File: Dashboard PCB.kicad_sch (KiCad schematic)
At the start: 32 parts, among them J1 Controls_Leader_Export_02x06, J2 Conn_01x02, J3 Conn_01x02, J4 FAN_CTRL_01x02

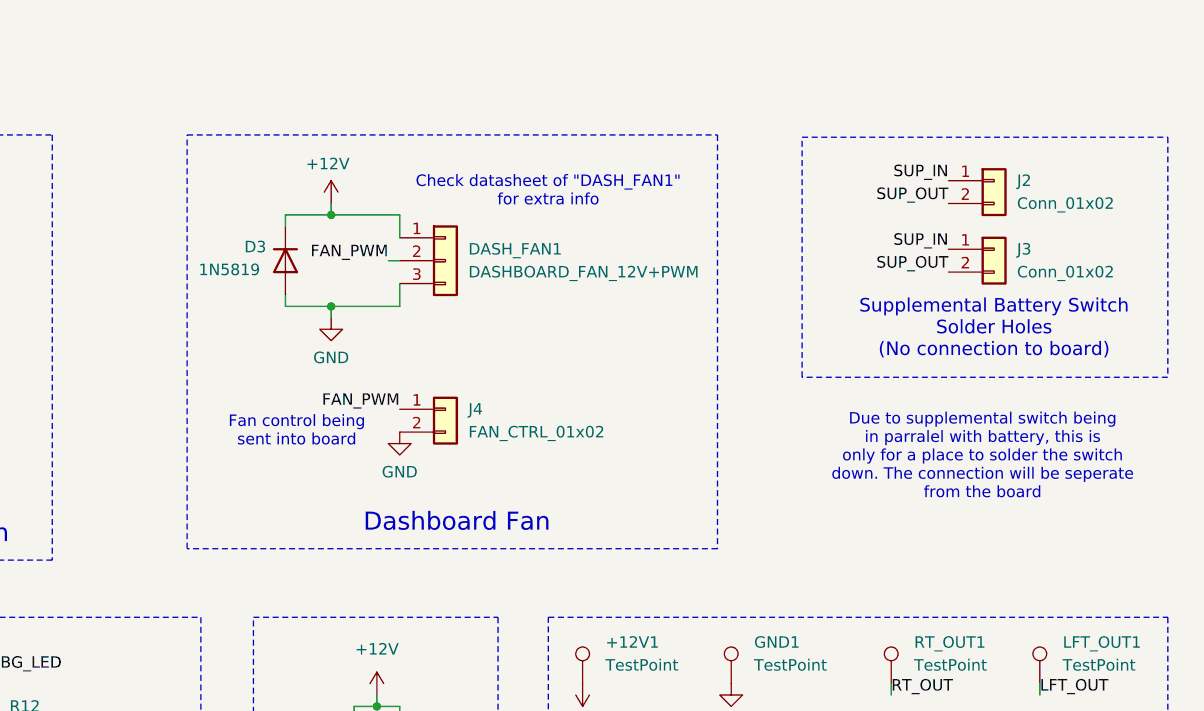
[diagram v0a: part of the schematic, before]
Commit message: Started assigning footprints
Still have a few missing, and not sure if im doing it all right
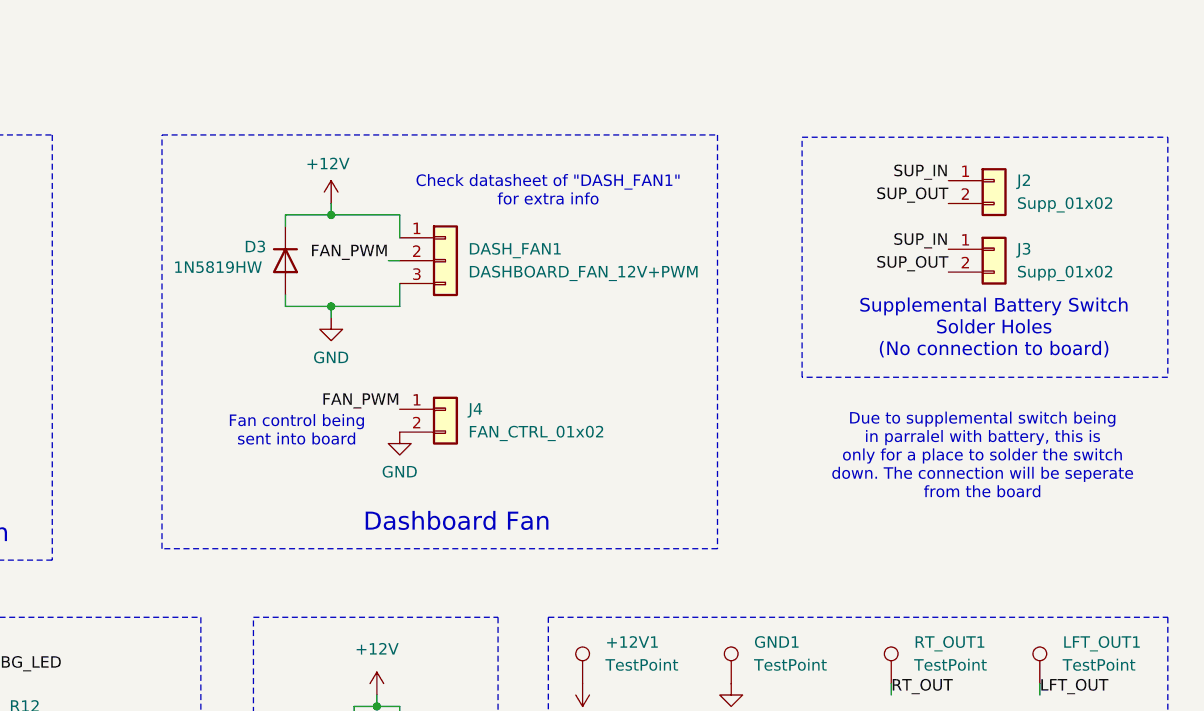
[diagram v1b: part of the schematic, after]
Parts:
- +12V1, CRUZ_EN1, CRUZ_SET1, DBG_LED1, FAN_PWM1, FWD_SW1, GND1, IGN_ARR1, IGN_PWR1, LFT_OUT1, REV_SW1, RT_OUT1: footprint (none) -> TestPoint:TestPoint_Plated_Hole_D3.0mm
- D3: value 1N5819 -> 1N5819HW; footprint (none) -> Diode_SMD:D_SOD-123
- DASH_FAN1: footprint (none) -> Connector_Molex:Molex_Micro-Fit_3.0_43650-0300_1x03_P3.00mm_Horizontal
- Heartbeat_LED1, LFT_LED1, RT_LED1: footprint (none) -> LED_SMD:LED_0805_2012Metric
- J1: footprint (none) -> Connector_Molex:Molex_Micro-Fit_3.0_43045-1200_2x06_P3.00mm_Horizontal
- J2, J3: value Conn_01x02 -> Supp_01x02
- J4: footprint (none) -> Connector_Molex:Molex_Micro-Fit_3.0_43650-0200_1x02_P3.00mm_Horizontal
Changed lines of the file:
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@@
 	)
 	(rectangle
-		(start 147.828 60.96)
+		(start 145.034 60.96)
 		(end 206.756 106.934)
 		(stroke
@@
 			)
 		)
-		(property "Footprint" ""
+		(property "Footprint" "TestPoint:TestPoint_Plated_Hole_D3.0mm"
 			(at 213.36 121.92 0)
 			(effects
@@
 			)
 		)
-		(property "Footprint" ""
+		(property "Footprint" "LED_SMD:LED_0805_2012Metric"
 			(at 97.79 133.35 0)
 			(effects
@@
 			)
 		)
-		(property "Footprint" ""
+		(property "Footprint" "TestPoint:TestPoint_Plated_Hole_D3.0mm"
 			(at 247.65 134.62 0)
 			(effects
@@
 			)
 		)
-		(property "Footprint" ""
+		(property "Footprint" "Connector_Molex:Molex_Micro-Fit_3.0_43650-0200_1x02_P3.00mm_Horizontal"
 			(at 176.53 91.44 0)
 			(effects
@@
 			)
 		)
-		(property "Value" "Conn_01x02"
+		(property "Value" "Supp_01x02"
 			(at 240.03 68.5799 0)
 			(effects
@@
 			)
 		)
-		(property "Footprint" ""
+		(property "Footprint" "TestPoint:TestPoint_Plated_Hole_D3.0mm"
 			(at 196.85 147.32 0)
 			(effects
@@
 			)
 		)
-		(property "Value" "Conn_01x02"
+		(property "Value" "Supp_01x02"
 			(at 240.03 76.1999 0)
 			(effects
@@
 			)
 		)
-		(property "Footprint" ""
+		(property "Footprint" "LED_SMD:LED_0805_2012Metric"
 			(at 71.12 133.35 0)
 			(effects
@@
 			)
 		)
-		(property "Footprint" ""
+		(property "Footprint" "TestPoint:TestPoint_Plated_Hole_D3.0mm"
 			(at 231.14 147.32 0)
 			(effects
@@
 			)
 		)
-		(property "Footprint" ""
+		(property "Footprint" "TestPoint:TestPoint_Plated_Hole_D3.0mm"
 			(at 213.36 147.32 0)
 			(effects
@@
 			)
 		)
-		(property "Value" "1N5819"
-			(at 149.098 75.946 90)
+		(property "Value" "1N5819HW"
+			(at 146.304 75.692 90)
 			(effects
 				(font
@@
 			)
 		)
-		(property "Footprint" ""
+		(property "Footprint" "Diode_SMD:D_SOD-123"
 			(at 158.75 74.93 0)
 			(effects
@@
 			)
 		)
-		(property "Datasheet" "~"
+		(property "Datasheet" "https://www.digikey.com/en/products/detail/diodes-incorporated/1N5819HW-7-F/814970"
 			(at 158.75 74.93 0)
 			(effects
@@
 			)
 		)
-		(property "Footprint" ""
+		(property "Footprint" "TestPoint:TestPoint_Plated_Hole_D3.0mm"
 			(at 196.85 121.92 0)
 			(effects
@@
 			)
 		)
-		(property "Footprint" ""
+		(property "Footprint" "TestPoint:TestPoint_Plated_Hole_D3.0mm"
 			(at 196.85 134.62 0)
 			(effects
@@
 			)
 		)
-		(property "Footprint" ""
+		(property "Footprint" "Connector_Molex:Molex_Micro-Fit_3.0_43650-0300_1x03_P3.00mm_Horizontal"
 			(at 176.53 74.93 0)
 			(effects
@@
 			)
 		)
-		(property "Footprint" ""
+		(property "Footprint" "Connector_Molex:Molex_Micro-Fit_3.0_43045-1200_2x06_P3.00mm_Horizontal"
 			(at 107.95 85.09 0)
 			(effects
@@
 			)
 		)
-		(property "Footprint" ""
+		(property "Footprint" "TestPoint:TestPoint_Plated_Hole_D3.0mm"
 			(at 213.36 134.62 0)
 			(effects
@@
 			)
 		)
-		(property "Footprint" ""
+		(property "Footprint" "TestPoint:TestPoint_Plated_Hole_D3.0mm"
 			(at 247.65 121.92 0)
 			(effects
@@
 			)
 		)
-		(property "Footprint" ""
+		(property "Footprint" "TestPoint:TestPoint_Plated_Hole_D3.0mm"
 			(at 247.65 147.32 0)
 			(effects
@@
 			)
 		)
-		(property "Footprint" ""
+		(property "Footprint" "TestPoint:TestPoint_Plated_Hole_D3.0mm"
 			(at 231.14 121.92 0)
 			(effects
@@
 			)
 		)
-		(property "Footprint" ""
+		(property "Footprint" "TestPoint:TestPoint_Plated_Hole_D3.0mm"
 			(at 231.14 134.62 0)
 			(effects
@@
 			)
 		)
-		(property "Footprint" ""
+		(property "Footprint" "LED_SMD:LED_0805_2012Metric"
 			(at 125.73 133.35 0)
 			(effects

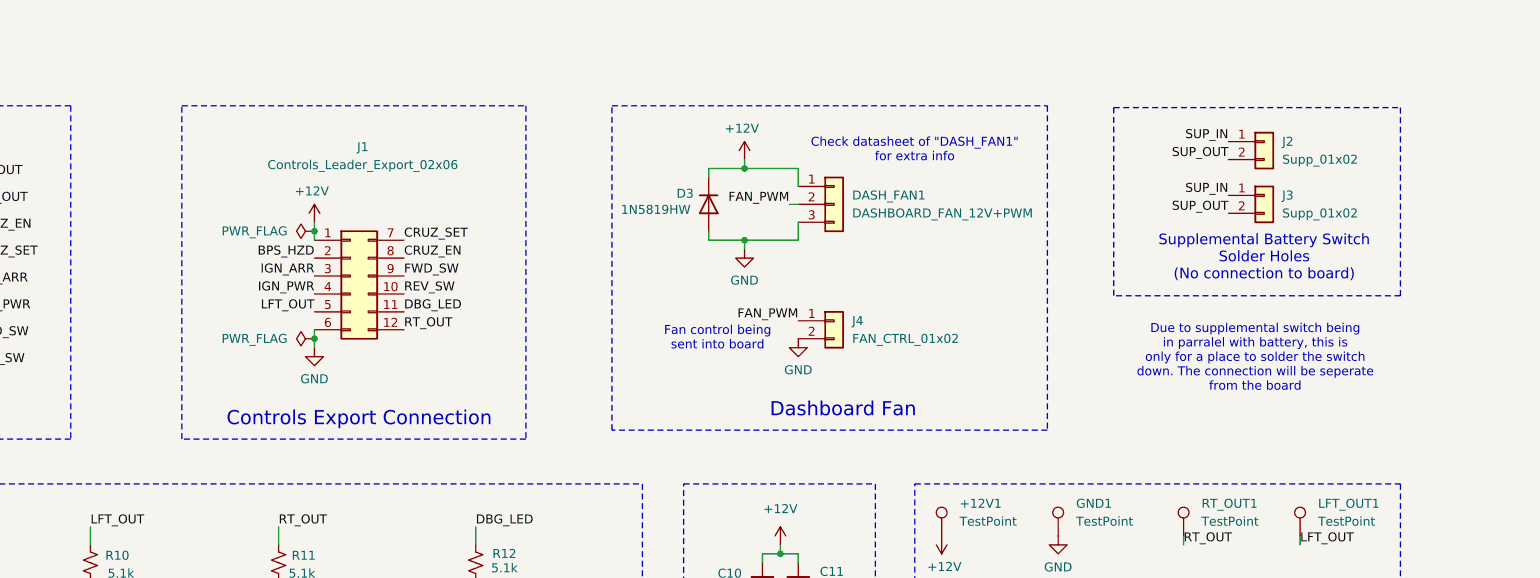
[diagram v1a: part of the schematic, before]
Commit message: Added a lot footprints
Some of them are custom and need to be double checked. Also no sure if they are all correctly included
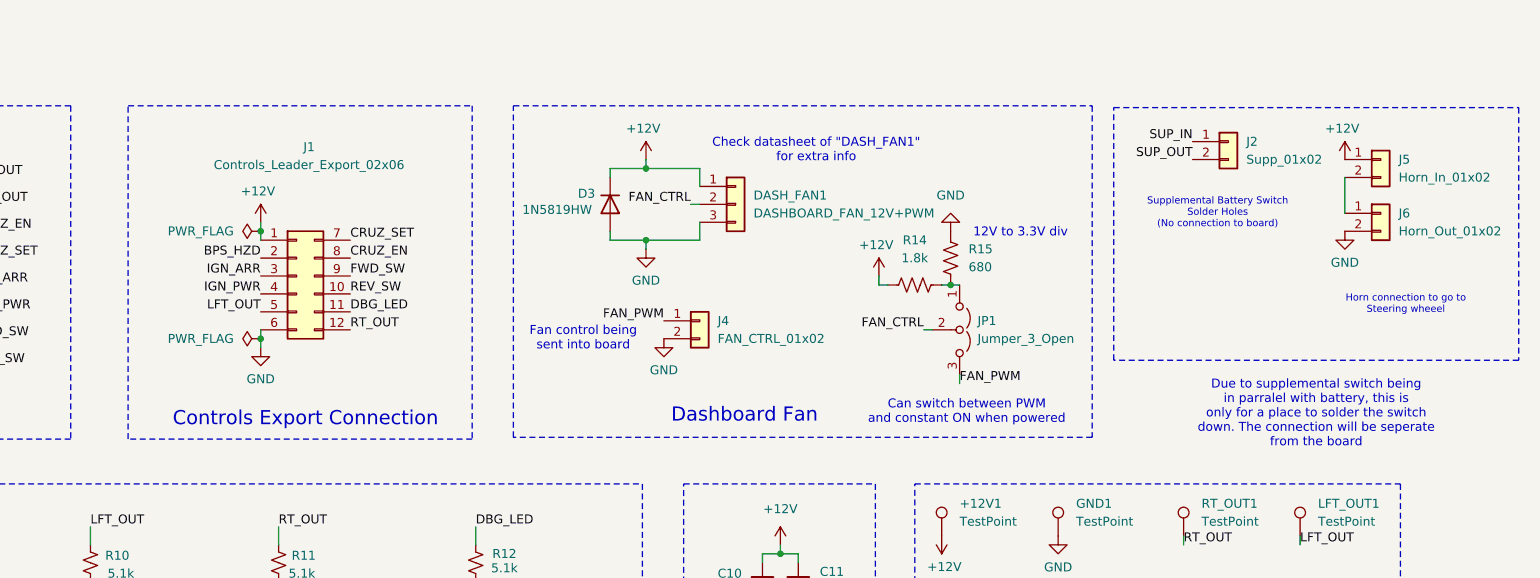
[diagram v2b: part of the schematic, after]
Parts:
- removed J3: Supp_01x02, symbol Connector_Generic:Conn_01x02
- added J5: Horn_In_01x02, Connector_Molex:Molex_Micro-Fit_3.0_43650-0200_1x02_P3.00mm_Horizontal, symbol Connector_Generic:Conn_01x02
- added J6: Horn_Out_01x02, Connector_Molex:Molex_Micro-Fit_3.0_43650-0200_1x02_P3.00mm_Horizontal, symbol Connector_Generic:Conn_01x02
- added JP1: Jumper_3_Open, Jumper:SolderJumper-3_P1.3mm_Open_RoundedPad1.0x1.5mm, symbol Jumper:Jumper_3_Open
- added R14: 1.8k, Resistor_SMD:R_0805_2012Metric, symbol Device:R_US
- added R15: 680, Resistor_SMD:R_0805_2012Metric, symbol Device:R_US
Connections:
- net +12V: now also J5.1 (Pin_1), R14.1
- net FAN_PWM: now also JP1.3 (B); no longer DASH_FAN1.2 (Pin_2)
- net GND: now also J6.2 (Pin_2), R15.2
- new net: JP1.1 (A), R14.2, R15.1
- new net: J5.2 (Pin_2), J6.1 (Pin_1)
- new net FAN_CTRL: DASH_FAN1.2 (Pin_2), JP1.2 (C)
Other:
- note added: "12V to 3.3V div"
- note added: "Can switch between PWM and constant ON when powered"
- note added: "Horn connection to go to Steering wheeel"
- moved on the sheet: D3, DASH_FAN1, J1, J2, J4
